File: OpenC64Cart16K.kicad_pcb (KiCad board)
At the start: 2 copper layers, 58.4 x 50.8 mm, 11 parts, among them J1 OSHW_LOGO, J2 PEG_HOLE, P1 CONN_01X03, P2 CONN_01X03, SW1 RESET_SW, U1 C64-Exp-Port, U2 27512

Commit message: Final touches for V1
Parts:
- SW1: value RESET_SW -> RESET
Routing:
- net Net-(U1-Pad18): track 37.0 -> 36.4 mm
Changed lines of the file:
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@@
   (title_block
     (title "OpenC64Cart16K: C64 Single-Chip 16K Cartridge")
-    (date 2018-01-02)
+    (date 2018-01-07)
     (rev 1)
     (company SukkoPera)
@@
     (39 F.Mask user)
     (44 Edge.Cuts user)
-    (49 F.Fab user hide)
+    (49 F.Fab user)
   )
   (setup
@@
     (pad 2 thru_hole circle (at 2.5 0 90) (size 1.6 1.6) (drill 0.8) (layers *.Cu *.Mask)
       (net 2 +5V))
-    (model Capacitors_SMD.3dshapes/C_0805.wrl
+    (model Capacitors_SMD.3dshapes/C_0805.wrl-xxx
       (at (xyz 0 0 0))
       (scale (xyz 1 1 1))
@@
       (effects (font (size 1.27 1.27) (thickness 0.3175)))
     )
-    (fp_text value RESET_SW (at -4.699 0 360) (layer F.SilkS)
+    (fp_text value RESET (at -4.53644 -0.0508 360) (layer F.SilkS)
       (effects (font (size 1.27 1.27) (thickness 0.254)))
     )
@@
   (segment (start 107.95 121.351726) (end 107.95 125.601726) (width 0.25) (layer F.Cu) (net 6))
   (segment (start 105.664 99.314) (end 105.664 100.66382) (width 0.25) (layer F.Cu) (net 7))
+  (segment (start 96.774 109.55382) (end 96.774 115.57) (width 0.25) (layer F.Cu) (net 7))
   (segment (start 105.664 100.66382) (end 96.774 109.55382) (width 0.25) (layer F.Cu) (net 7))
-  (segment (start 96.774 109.55382) (end 96.774 115.57) (width 0.25) (layer F.Cu) (net 7))
+  (segment (start 103.359789 117.329789) (end 105.41 119.38) (width 0.25) (layer F.Cu) (net 7))
   (segment (start 96.774 115.57) (end 98.533789 117.329789) (width 0.25) (layer F.Cu) (net 7))
-  (segment (start 98.533789 117.329789) (end 104.375789 117.329789) (width 0.25) (layer F.Cu) (net 7))
-  (segment (start 104.375789 117.329789) (end 105.41 118.364) (width 0.25) (layer F.Cu) (net 7))
-  (segment (start 105.41 118.364) (end 105.41 125.601726) (width 0.25) (layer F.Cu) (net 7))
+  (segment (start 105.41 119.38) (end 105.41 125.601726) (width 0.25) (layer F.Cu) (net 7))
+  (segment (start 98.533789 117.329789) (end 103.359789 117.329789) (width 0.25) (layer F.Cu) (net 7))
   (segment (start 102.87 125.601726) (end 102.87 118.11) (width 0.25) (layer F.Cu) (net 8))
   (segment (start 102.87 118.11) (end 102.5398 117.7798) (width 0.25) (layer F.Cu) (net 8))

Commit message: Fix cap value
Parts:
- C1: value C -> 100n
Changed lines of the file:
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@@
     (links 51)
     (no_connects 0)
-    (area 59.614999 78.664999 118.185001 129.615001)
+    (area 55.174287 78.664999 134.85 147.480001)
     (thickness 1.6)
     (drawings 18)
@@
       (effects (font (size 1 1) (thickness 0.15)))
     )
-    (fp_text value C (at 0 1.75 90) (layer F.Fab)
+    (fp_text value 100n (at 0 1.75 90) (layer F.Fab)
       (effects (font (size 1 1) (thickness 0.15)))
     )

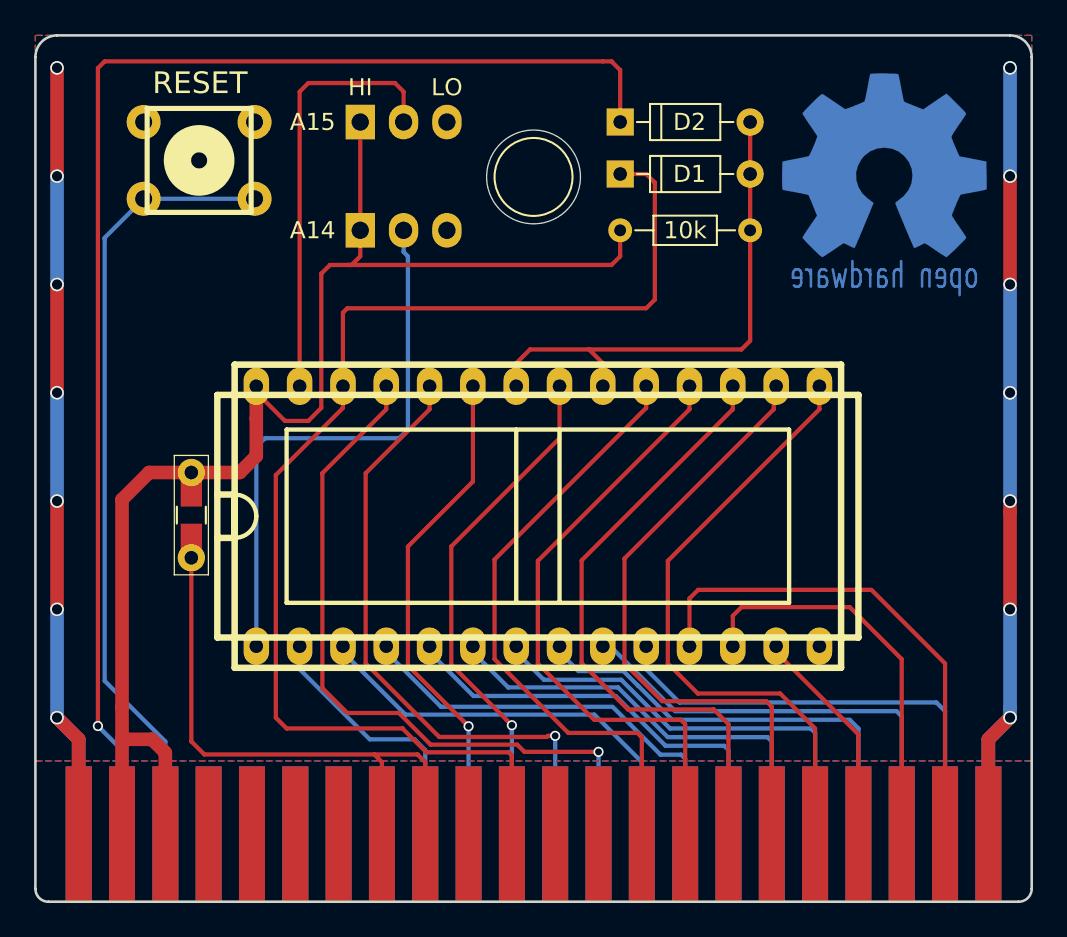
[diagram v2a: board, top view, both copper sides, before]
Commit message: Use THT/SMD combo pads for all components
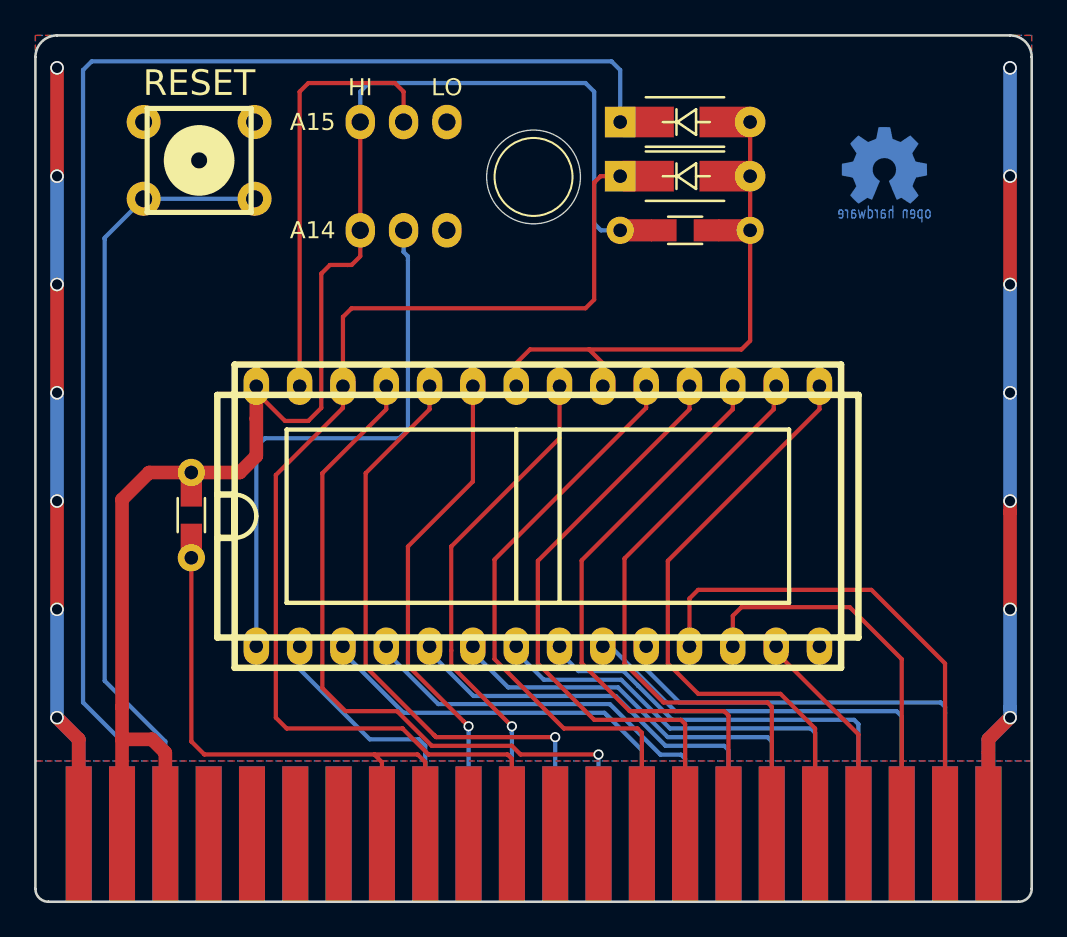
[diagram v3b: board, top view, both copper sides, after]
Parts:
- D1, D2: footprint Diodes_THT:D_DO-35_SOD27_P7.62mm_Horizontal -> OpenC64Cart16K:D_DO35+SMA
- J1: footprint w_logo:Logo_copper_OSHW_12x13mm -> w_logo:Logo_copper_OSHW_6x6mm
- R1: footprint Resistors_THT:R_Axial_DIN0204_L3.6mm_D1.6mm_P7.62mm_Horizontal -> OpenC64Cart16K:R_0805+THT-7.62mm
- SW1: value RESET -> RESET_SW
- moved R1 3.81 mm to (97.8, 90.2)
- moved D1 0.13 mm to (94.0, 87.0)
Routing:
- net +5V: track 82.9 -> 93.9 mm
- net Net-(D1-Pad2): track 30.9 -> 37.0 mm
- net Net-(D2-Pad1): track 79.6 -> 82.4 mm, vias 1 -> 0
- net Net-(D1-Pad1): track 72.5 -> 69.8 mm
- net Net-(U1-PadR): track 24.8 -> 25.6 mm
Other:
- board text added: "RESET"
- board text added: "V2"
- board text removed: "V1"
